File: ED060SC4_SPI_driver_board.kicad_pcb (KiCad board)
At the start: 2 copper layers, 84 parts, among them J1 ED060SC4, J2 Conn_01x06, J3 Conn_01x04, J4 Conn_01x04, SW1 SS12D07VG2, SW2 DSIC01LSGET, U1 TPS65185RGZR, U2 STM32F103C8T6, U3 USBLC6-4SC6, U4 USBLC6-2SC6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

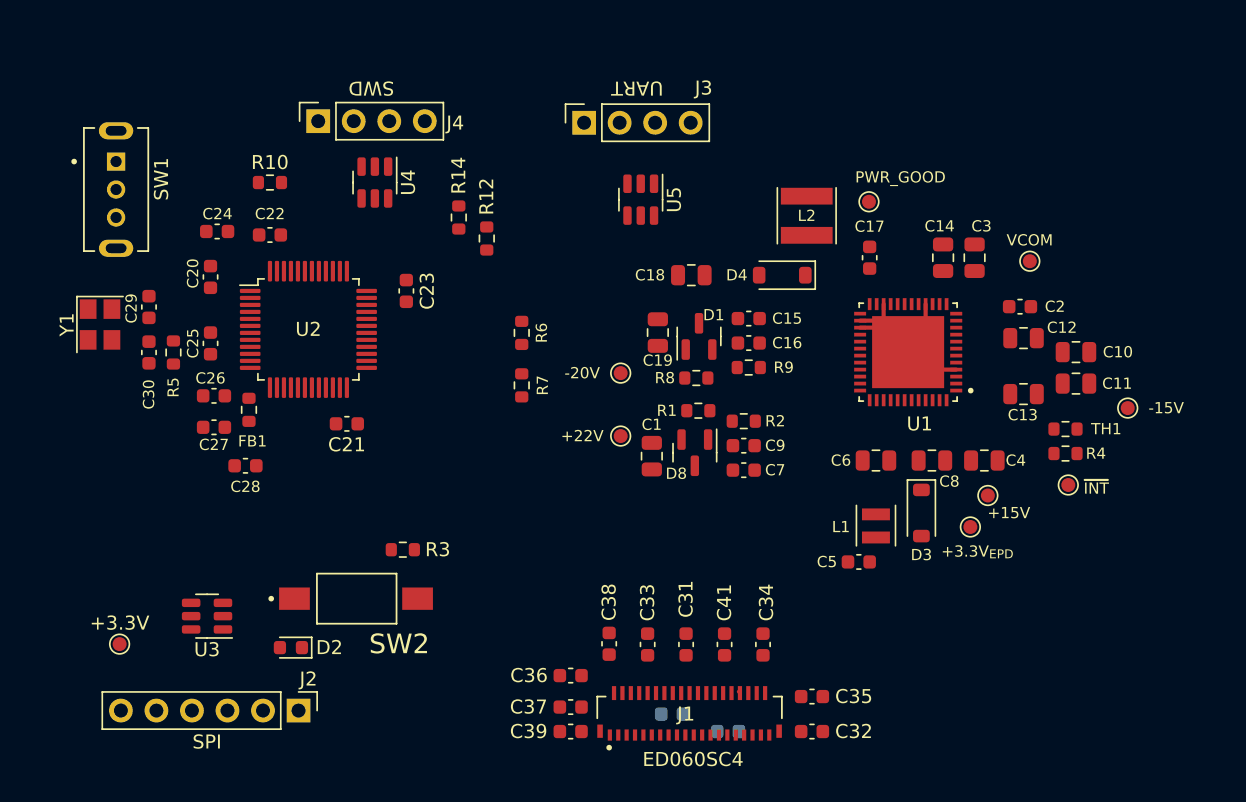
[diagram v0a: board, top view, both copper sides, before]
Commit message: Add a connector for easy access to voltages
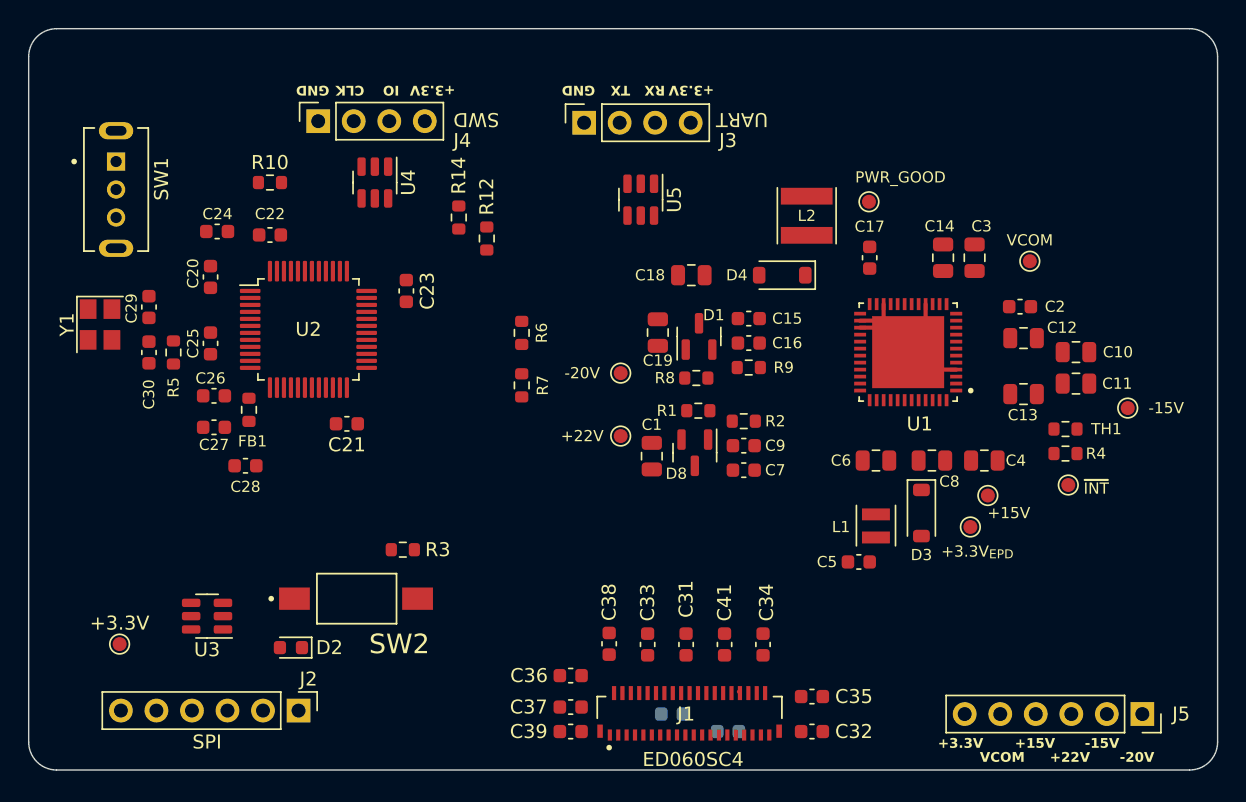
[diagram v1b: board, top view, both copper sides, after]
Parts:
- added J5: Conn_01x06, Connector_PinSocket_2.54mm:PinSocket_1x06_P2.54mm_Vertical, F.Cu at (127.6, 96.0)
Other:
- board outline added: 85 x 53 mm
- board text added: "+15V"
- board text added: "+22V"
- board text added: "+3.3V"
- board text added: "-15V"
- board text added: "-20V"
- board text added: "CLK"
- board text added: "GND"
- board text added: "IO"
- board text added: "RX"
- board text added: "TX"
- board text added: "VCOM"
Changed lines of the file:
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@@
     (pad_to_mask_clearance 0)
     (pcbplotparams
-      (layerselection 0x00010fc_ffffffff)
+      (layerselection 0x00010f4_ffffffff)
       (plot_on_all_layers_selection 0x0000000_00000000)
       (disableapertmacros false)
@@
       (outputformat 1)
       (mirror false)
-      (drillshape 1)
+      (drillshape 0)
       (scaleselection 1)
-      (outputdirectory "")
+      (outputdirectory "outputs/gerbers/")
     )
   )
@@
       (net 73 "+22V") (pinfunction "1") (pintype "passive"))
   )
+  (footprint "Connector_PinSocket_2.54mm:PinSocket_1x06_P2.54mm_Vertical" (layer "F.Cu")
+    (at 127.62 96 -90)
+    (descr "Through hole straight socket strip, 1x06, 2.54mm pitch, single row (from Kicad 4.0.7), script generated")
+    (tags "Through hole socket strip THT 1x06 2.54mm single row")
+    (property "Sheetfile" "ED060SC4_SPI_driver_board.kicad_sch")
+    (property "Sheetname" "")
+    (property "ki_description" "Generic connector, single row, 01x06, script generated (kicad-library-utils/schlib/autogen/connector/)")
+    (property "ki_keywords" "connector")
+    (attr through_hole)
+    (fp_text reference "J5" (at 0 -2.77 -180) (layer "F.SilkS")
+        (effects (font (size 1 1) (thickness 0.15)))
+    )
+    (fp_text value "Conn_01x06" (at 0 15.47 90) (layer "F.Fab") hide
+        (effects (font (size 1 1) (thickness 0.15)))
+    )
+    (fp_text user "${REFERENCE}" (at 0 6.35) (layer "F.Fab") hide
+        (effects (font (size 1 1) (thickness 0.15)))
+    )
+    (fp_line (start -1.33 1.27) (end -1.33 14.03)
+      (stroke (width 0.12) (type solid)) (layer "F.SilkS"))
+    (fp_line (start -1.33 1.27) (end 1.33 1.27)
+      (stroke (width 0.12) (type solid)) (layer "F.SilkS"))
+    (fp_line (start -1.33 14.03) (end 1.33 14.03)
+      (stroke (width 0.12) (type solid)) (layer "F.SilkS"))
+    (fp_line (start 0 -1.33) (end 1.33 -1.33)
+      (stroke (width 0.12) (type solid)) (layer "F.SilkS"))
+    (fp_line (start 1.33 -1.33) (end 1.33 0)
+      (stroke (width 0.12) (type solid)) (layer "F.SilkS"))
+    (fp_line (start 1.33 1.27) (end 1.33 14.03)
+      (stroke (width 0.12) (type solid)) (layer "F.SilkS"))
+    (fp_line (start -1.8 -1.8) (end 1.75 -1.8)
+      (stroke (width 0.05) (type solid)) (layer "F.CrtYd"))
+    (fp_line (start -1.8 14.45) (end -1.8 -1.8)
+      (stroke (width 0.05) (type solid)) (layer "F.CrtYd"))
+    (fp_line (start 1.75 -1.8) (end 1.75 14.45)
+      (stroke (width 0.05) (type solid)) (layer "F.CrtYd"))
+    (fp_line (start 1.75 14.45) (end -1.8 14.45)
+      (stroke (width 0.05) (type solid)) (layer "F.CrtYd"))
+    (fp_line (start -1.27 -1.27) (end 0.635 -1.27)
+      (stroke (width 0.1) (type solid)) (layer "F.Fab"))
+    (fp_line (start -1.27 13.97) (end -1.27 -1.27)
+      (stroke (width 0.1) (type solid)) (layer "F.Fab"))
+    (fp_line (start 0.635 -1.27) (end 1.27 -0.635)
+      (stroke (width 0.1) (type solid)) (layer "F.Fab"))
+    (fp_line (start 1.27 -0.635) (end 1.27 13.97)
+      (stroke (width 0.1) (type solid)) (layer "F.Fab"))
+    (fp_line (start 1.27 13.97) (end -1.27 13.97)
+      (stroke (width 0.1) (type solid)) (layer "F.Fab"))
+    (pad "1" thru_hole rect (at 0 0 270) (size 1.7 1.7) (drill 1) (layers "*.Cu" "*.Mask")
+      (net 75 "-20V") (pinfunction "Pin_1") (pintype "passive"))
+    (pad "2" thru_hole oval (at 0 2.54 270) (size 1.7 1.7) (drill 1) (layers "*.Cu" "*.Mask")
+      (net 72 "-15V") (pinfunction "Pin_2") (pintype "passive"))
+    (pad "3" thru_hole oval (at 0 5.08 270) (size 1.7 1.7) (drill 1) (layers "*.Cu" "*.Mask")
+      (net 73 "+22V") (pinfunction "Pin_3") (pintype "passive"))
+    (pad "4" thru_hole oval (at 0 7.62 270) (size 1.7 1.7) (drill 1) (layers "*.Cu" "*.Mask")
+      (net 57 "+15V") (pinfunction "Pin_4") (pintype "passive"))
+    (pad "5" thru_hole oval (at 0 10.16 270) (size 1.7 1.7) (drill 1) (layers "*.Cu" "*.Mask")
+      (net 74 "VCOM") (pinfunction "Pin_5") (pintype "passive"))
+    (pad "6" thru_hole oval (at 0 12.7 270) (size 1.7 1.7) (drill 1) (layers "*.Cu" "*.Mask")
+      (net 76 "+3.3V_{EPD}") (pinfunction "Pin_6") (pintype "passive"))
+    (model "${KICAD6_3DMODEL_DIR}/Connector_PinSocket_2.54mm.3dshapes/PinSocket_1x06_P2.54mm_Vertical.wrl"
+      (offset (xyz 0 0 0))
+      (scale (xyz 1 1 1))
+      (rotate (xyz 0 0 0))
+    )
+  )
   (footprint "Capacitor_SMD:C_0603_1608Metric" (layer "F.Cu")
     (at 61 69.5 90)
@@
     (property "ki_keywords" "connector")
     (attr through_hole)
-    (fp_text reference "J3" (at 2.475 8.55) (layer "F.SilkS")
+    (fp_text reference "J3" (at -1.275 10.29 180) (layer "F.SilkS")
         (effects (font (size 1 1) (thickness 0.15)))
     )
@@
         (effects (font (size 1 1) (thickness 0.15)))
     )
-    (fp_text user "UART" (at 2.475 3.8 180 unlocked) (layer "F.SilkS")
+    (fp_text user "UART" (at 0.225 11.29 180 unlocked) (layer "F.SilkS")
         (effects (font (size 1 1) (thickness 0.15)))
     )
@@
     (property "ki_keywords" "connector")
     (attr through_hole)
-    (fp_text reference "J4" (at -0.1375 9.8 180) (layer "F.SilkS")
+    (fp_text reference "J4" (at -1.3875 10.3 180) (layer "F.SilkS")
         (effects (font (size 1 1) (thickness 0.15)))
     )
@@
         (effects (font (size 1 1) (thickness 0.15)))
     )
-    (fp_text user "SWD" (at 2.3625 3.8 180 unlocked) (layer "F.SilkS")
+    (fp_text user "SWD" (at 0.1125 11.3 180 unlocked) (layer "F.SilkS")
         (effects (font (size 1 1) (thickness 0.15)))
     )
@@
     )
   )
+  (gr_arc (start 50 100) (mid 48.585786 99.414214) (end 48 98)
+    (stroke (width 0.1) (type default)) (layer "Edge.Cuts"))
+  (gr_arc (start 133 98) (mid 132.414214 99.414214) (end 131 100)
+    (stroke (width 0.1) (type default)) (layer "Edge.Cuts"))
+  (gr_line (start 131 100) (end 50 100)
+    (stroke (width 0.1) (type default)) (layer "Edge.Cuts"))
+  (gr_arc (start 131 47) (mid 132.414214 47.585786) (end 133 49)
+    (stroke (width 0.1) (type default)) (layer "Edge.Cuts"))
+  (gr_line (start 133 49) (end 133 98)
+    (stroke (width 0.1) (type default)) (layer "Edge.Cuts"))
+  (gr_line (start 50 47) (end 131 47)
+    (stroke (width 0.1) (type default)) (layer "Edge.Cuts"))
+  (gr_line (start 48 98) (end 48 49)
+    (stroke (width 0.1) (type default)) (layer "Edge.Cuts"))
+  (gr_arc (start 48 49) (mid 48.585786 47.585786) (end 50 47)
+    (stroke (width 0.1) (type default)) (layer "Edge.Cuts"))
+  (gr_text "+3.3V" (at 78.5 51 180) (layer "F.SilkS")
+    (effects (font (size 0.7 0.7) (thickness 0.15) bold) (justify left bottom))
+  )
+  (gr_text "+3.3V\n" (at 113 98.5) (layer "F.SilkS")
+    (effects (font (size 0.7 0.7) (thickness 0.15) bold) (justify left bottom))
+  )
+  (gr_text "TX" (at 91 51 180) (layer "F.SilkS")
+    (effects (font (size 0.7 0.7) (thickness 0.15) bold) (justify left bottom))
+  )
+  (gr_text "GND" (at 69.5 51 180) (layer "F.SilkS")
+    (effects (font (size 0.7 0.7) (thickness 0.15) bold) (justify left bottom))
+  )
+  (gr_text "VCOM" (at 116 99.5) (layer "F.SilkS")
+    (effects (font (size 0.7 0.7) (thickness 0.15) bold) (justify left bottom))
+  )
+  (gr_text "GND" (at 88.5 51 180) (layer "F.SilkS")
+    (effects (font (size 0.7 0.7) (thickness 0.15) bold) (justify left bottom))
+  )
+  (gr_text "CLK" (at 72 51 180) (layer "F.SilkS")
+    (effects (font (size 0.7 0.7) (thickness 0.15) bold) (justify left bottom))
+  )
+  (gr_text "+3.3V" (at 97 51 180) (layer "F.SilkS")
+    (effects (font (size 0.7 0.7) (thickness 0.15) bold) (justify left bottom))
+  )
+  (gr_text "-20V" (at 126 99.5) (layer "F.SilkS")
+    (effects (font (size 0.7 0.7) (thickness 0.15) bold) (justify left bottom))
+  )
+  (gr_text "+15V\n" (at 118.5 98.5) (layer "F.SilkS")
+    (effects (font (size 0.7 0.7) (thickness 0.15) bold) (justify left bottom))
+  )
+  (gr_text "-15V" (at 123.5 98.5) (layer "F.SilkS")
+    (effects (font (size 0.7 0.7) (thickness 0.15) bold) (justify left bottom))
+  )
+  (gr_text "RX\n" (at 93.5 51 180) (layer "F.SilkS")
+    (effects (font (size 0.7 0.7) (thickness 0.15) bold) (justify left bottom))
+  )
+  (gr_text "IO" (at 74.5 51 180) (layer "F.SilkS")
+    (effects (font (size 0.7 0.7) (thickness 0.15) bold) (justify left bottom))
+  )
+  (gr_text "+22V" (at 121 99.5) (layer "F.SilkS")
+    (effects (font (size 0.7 0.7) (thickness 0.15) bold) (justify left bottom))
+  )
   (segment (start 98.85 94.5) (end 98.75 94.4) (width 0.25) (layer "F.Cu") (net 35))
   (segment (start 114.31 71.375) (end 112.125 71.375) (width 0.3) (layer "F.Cu") (net 77))
@@
     )
   )
-  (group "" (id 9d04a714-b505-42f1-aae5-480f09be72f2)
-    (members
-      8bed0448-f9a7-4069-8e95-a58eb71c0f1f
-      cb300bf4-5fab-4072-9c6e-017fb00bb31e
-    )
-  )
-  (group "" (id b2b12437-e7a7-43b4-9527-af60ef82d0c2)
-    (members
-      3d59d22d-5684-48fa-b8e5-39c72f133de7
-      4432fb5d-1936-480e-95a2-18e9d6738e21
-    )
-  )

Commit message: PCB routing
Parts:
- moved TP4 16.4 mm to (112.5, 65.8)
- moved J5 14.4 mm to (113.9, 91.5)
- moved C5 14.0 mm to (93.9, 81.4), turned to -90 degrees
- moved C40 13.3 mm to (87.0, 89.8)
- moved C35 12.6 mm to (93.6, 87.8)
- moved C10 12.2 mm to (110.8, 69.0)
- moved C11 12.2 mm to (110.8, 71.2)
- moved C12 12.2 mm to (107.0, 68.0)
- moved C13 12.2 mm to (107.0, 72.0)
- moved C14 12.2 mm to (101.2, 62.2)
- moved C17 12.2 mm to (96.0, 62.2)
- moved C2 12.2 mm to (106.8, 65.8)
- moved C3 12.2 mm to (103.5, 62.2)
- moved C4 12.2 mm to (104.2, 76.8)
- moved C6 12.2 mm to (96.5, 76.8)
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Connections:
- U3 pad 1: /SPI1_MOSI -> /SPI1_MISO
- U3 pad 3: /SPI1_MISO -> /SPI1_MOSI
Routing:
- net GND: track 0.00 -> 107.5 mm, vias 0 -> 67
- net VCOM: track 0.00 -> 76.6 mm, vias 0 -> 3
- net -15V: track 0.00 -> 76.6 mm
- net +3.3V: track 0.00 -> 69.4 mm, vias 0 -> 21
- net /EPD_OE: track 0.00 -> 63.5 mm, vias 0 -> 4
- net +3.3V_{EPD}: track 0.00 -> 63.3 mm, vias 0 -> 7
- net -20V: track 0.00 -> 60.8 mm, vias 0 -> 4
- net /D1: track 0.00 -> 60.3 mm, vias 0 -> 4
- net /D5: track 0.00 -> 59.2 mm, vias 0 -> 4
- net /TPS_~{INT}: track 0.00 -> 57.9 mm, vias 0 -> 5
- net /EPD_SPV: track 0.14 -> 57.5 mm, vias 0 -> 7
- net +15V: track 0.00 -> 53.9 mm, vias 0 -> 2
- net /D0: track 0.00 -> 53.5 mm, vias 0 -> 4
- net +22V: track 0.00 -> 50.2 mm, vias 0 -> 2
- net /TPS_WAKEUP: track 0.00 -> 48.7 mm, vias 0 -> 2
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- added copper zone on In2.Cu, net +3.3V
- added copper zone on In2.Cu, net +3.3V_{EPD}
- added copper zone on F.Cu, net /EPD Power Rails/VB
- added copper zone on In1.Cu, net GND
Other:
- board size 85 x 53 mm -> 71.2 x 49 mm
- copper layers 2 -> 4
- board text added: "MISO"
- board text added: "MOSI"
- board text added: "SCK"
- board text added: "~{CS}"

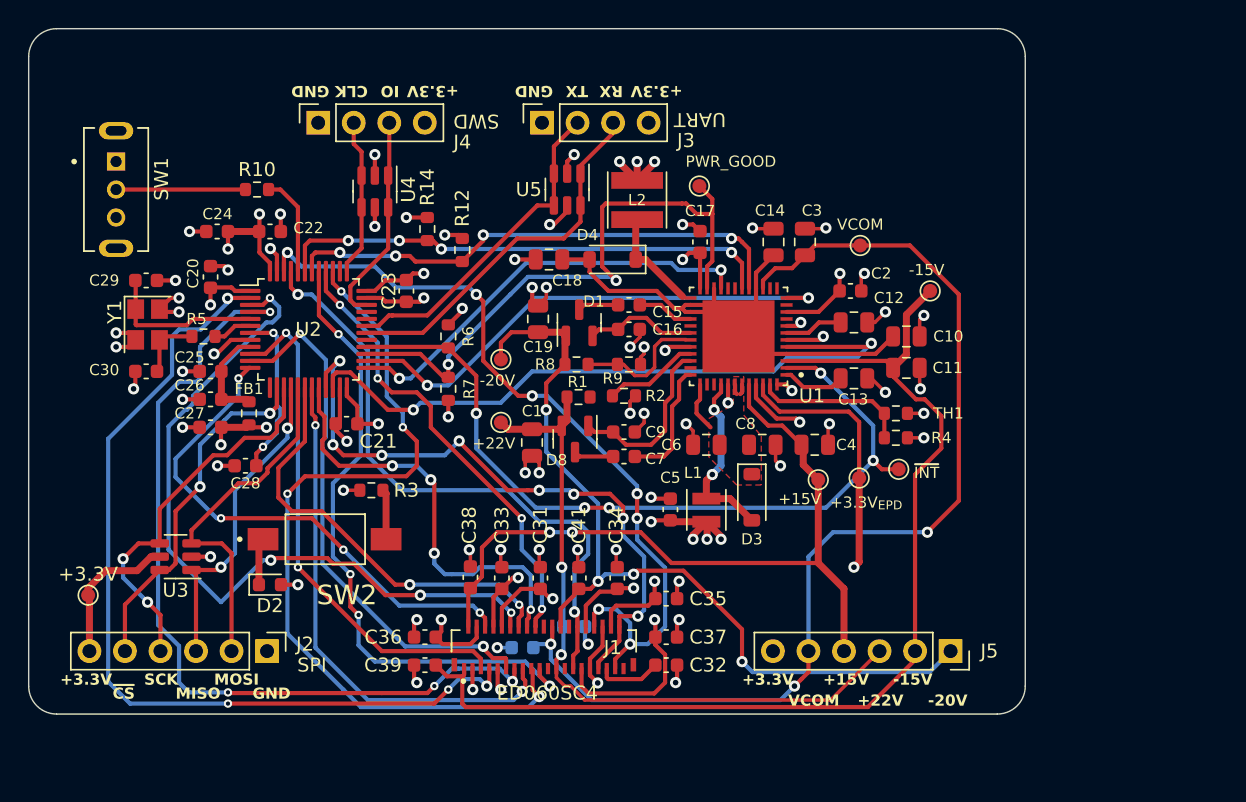
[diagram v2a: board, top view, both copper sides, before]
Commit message: Routed PCB + outputs
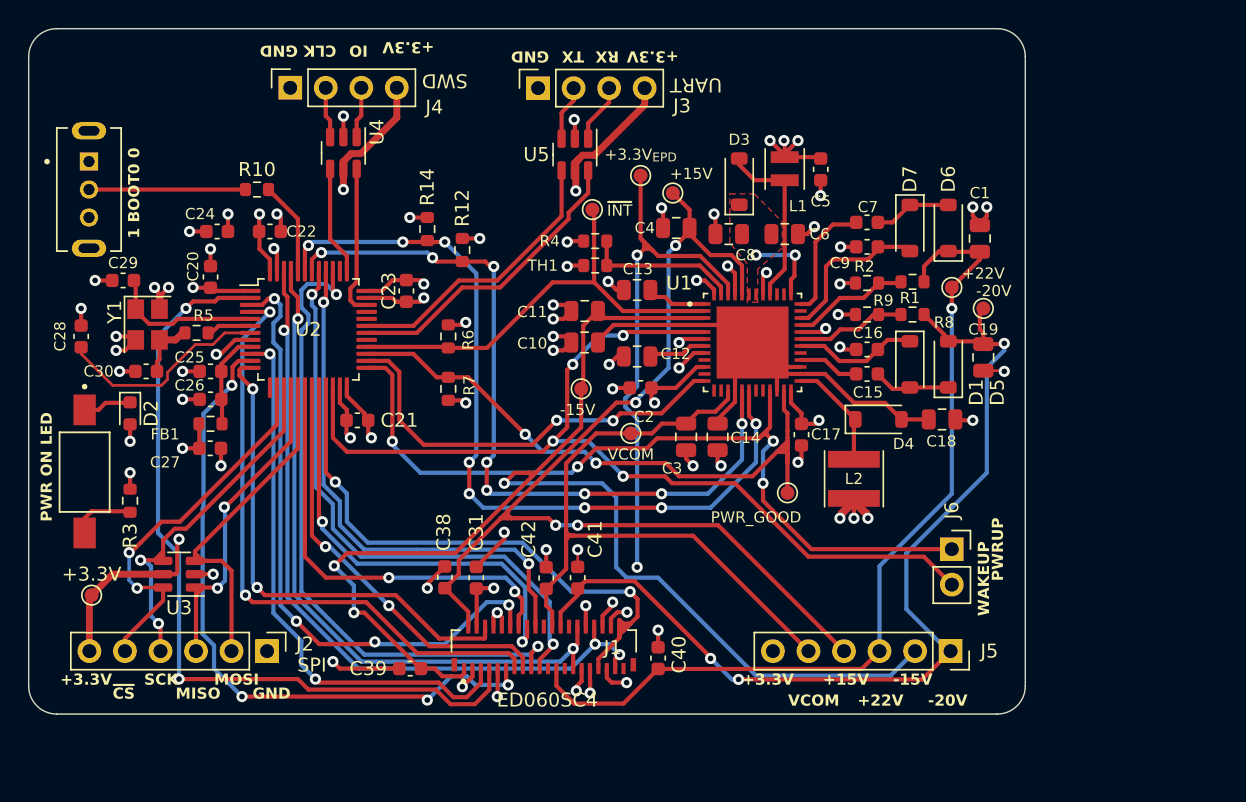
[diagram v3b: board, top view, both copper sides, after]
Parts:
- removed C32, C33, C34, C35, C36, C37: 100nF, Capacitor_SMD:C_0603_1608Metric
- removed D8: D_Dual_Series_AKC, Package_TO_SOT_SMD:SOT-23
- added D5: D, Diode_SMD:D_SOD-123, F.Cu at (113.8, 71.0)
- added D6: D, Diode_SMD:D_SOD-123, F.Cu at (113.8, 61.2)
- added D7: D, Diode_SMD:D_SOD-123, F.Cu at (111.0, 61.2)
- added J6: Conn_01x02, Connector_PinSocket_2.54mm:PinSocket_1x02_P2.54mm_Vertical, F.Cu at (114.0, 84.2)
- C40, C42: moved to F.Cu
- D1: value D_Dual_Series_AKC -> D; footprint Package_TO_SOT_SMD:SOT-23 -> Diode_SMD:D_SOD-123
- moved C1 35.2 mm to (116.0, 62.0), turned to -90 degrees
- moved TP6 34.7 mm to (116.2, 67.0), turned to 0 degrees
- moved TP5 33.7 mm to (114.0, 65.5), turned to 180 degrees
- moved C19 32.0 mm to (116.2, 70.5), turned to 90 degrees
- moved C18 30.3 mm to (113.3, 74.9), turned to 180 degrees
- moved TP9 28.7 mm to (88.3, 59.9), turned to 180 degrees
- moved L1 26.8 mm to (106.1, 57.7), turned to -90 degrees
- moved TP2 26.7 mm to (91.8, 57.5)
- moved C5 26.6 mm to (104.6, 57.1), turned to 90 degrees
- moved TP4 25.9 mm to (87.5, 72.8), turned to 180 degrees
- moved R4 25.7 mm to (88.5, 62.2), turned to 0 degrees
- moved R1 25.3 mm to (111.2, 65.1), turned to 0 degrees
- moved L2 25.3 mm to (107.0, 79.2), turned to 90 degrees
- moved R8 24.3 mm to (111.2, 67.4), turned to 0 degrees
- moved C7 24.1 mm to (107.9, 60.8), turned to 180 degrees
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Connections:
- D1 pad 1: -20V -> /EPD Power Rails/VEE_D
- D1 pad 2: /EPD Power Rails/VEE_D -> /EPD Power Rails/vee_drv_0
- J3 pad 2: /USART1_TX -> /USART1_TX_conn
- J3 pad 3: /USART1_RX -> /USART1_RX_conn
- J4 pad 2: /SWCLK -> /SWCLK_conn
- J4 pad 3: /SWDIO -> /SWDIO_conn
- U4 pad 1: /SWDIO -> /SWDIO_conn
- U4 pad 3: /SWCLK -> /SWCLK_conn
- U5 pad 1: /USART1_RX -> /USART1_RX_conn
- U5 pad 3: /USART1_TX -> /USART1_TX_conn
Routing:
- net /TPS_PWRUP: track 30.6 -> 59.9 mm, vias 2 -> 4
- net VCOM: track 76.6 -> 48.4 mm, vias 3 -> 0
- net /TPS_~{INT}: track 57.9 -> 32.2 mm, vias 5 -> 0
- net /I2C1_SDA: track 35.7 -> 58.6 mm, vias 4 -> 8
- net +15V: track 53.9 -> 76.8 mm, vias 2 -> 4
- net /TPS_WAKEUP: track 48.7 -> 69.4 mm, vias 2 -> 4
- net /I2C1_SCL: track 37.0 -> 55.0 mm, vias 4 -> 8
- net -15V: track 76.6 -> 94.3 mm, vias 0 -> 3
- net /D1: track 60.3 -> 44.4 mm, vias 4 -> 2
- net +22V: track 50.2 -> 63.5 mm, vias 2 -> 1
- net /D5: track 59.2 -> 47.5 mm, vias 4 -> 2
- net +3.3V_{EPD}: track 63.3 -> 51.9 mm, vias 7 -> 8
- net +3.3V: track 69.4 -> 80.1 mm, vias 21 -> 20
- net /EPD_SPH: track 38.4 -> 48.4 mm, vias 2 -> 4
- net -20V: track 60.8 -> 69.6 mm, vias 4 -> 3
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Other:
- board text added: "1 BOOT0 0"
- board text added: "PWR ON LED"
- board text added: "PWRUP"
- board text added: "WAKEUP"
